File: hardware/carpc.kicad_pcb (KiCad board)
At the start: 2 copper layers, 47 parts, among them IC1 ATMEGA328-P, K3 CANBus, P1 PWR_IN, P2 MELBUS, P3 CONN_4, P4 RTI, P5 RELAY_OUT, Q1 BC547, Q2 RELAY, Q3 BC547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

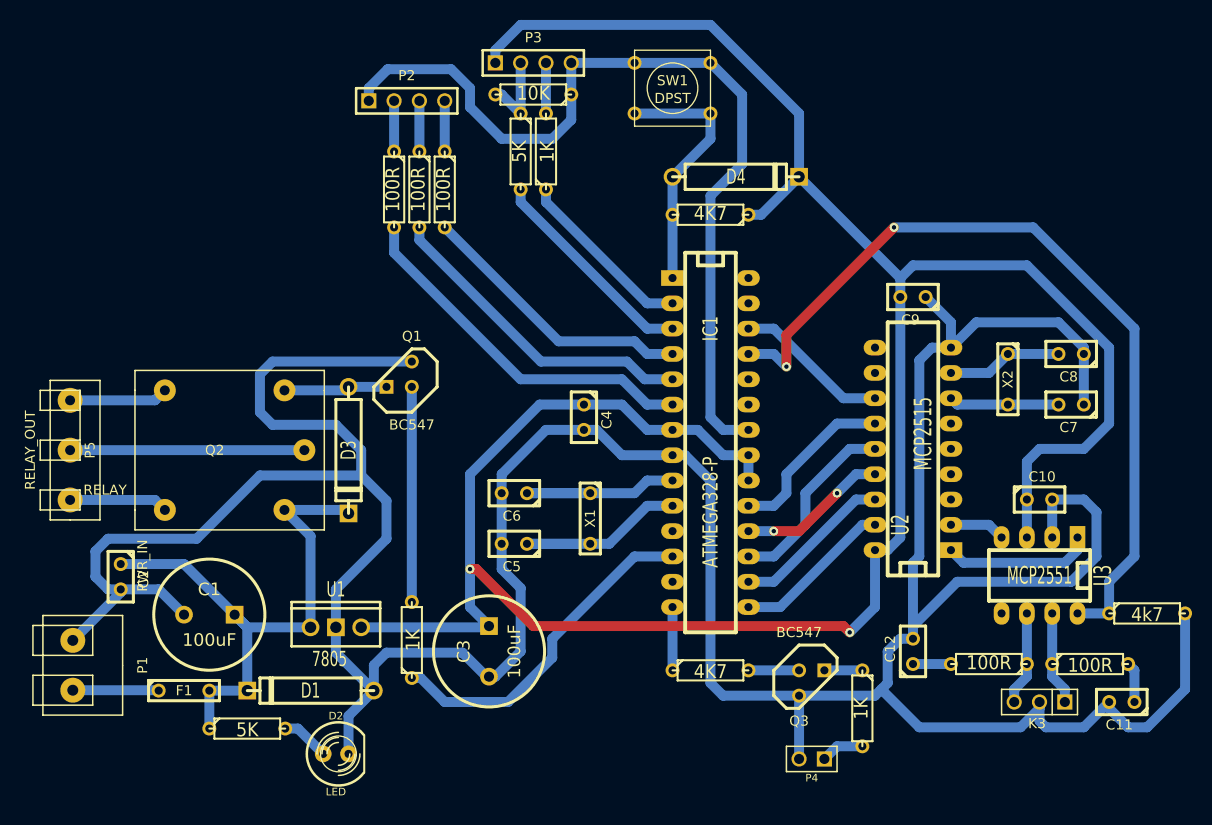
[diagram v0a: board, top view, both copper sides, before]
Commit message: Finished PCB layout
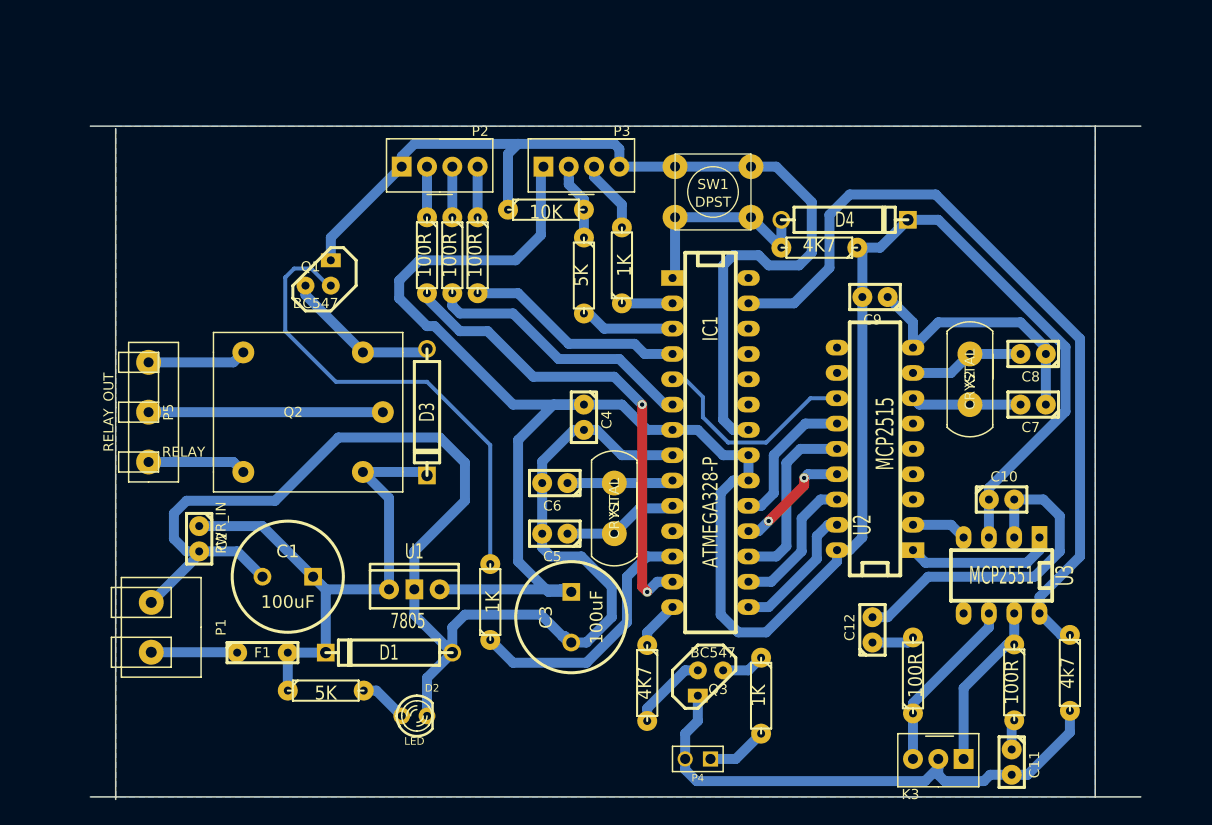
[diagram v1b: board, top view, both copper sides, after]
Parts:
- D2: footprint LED-5MM -> LED-3MM
- Q1, Q3: footprint TO92 -> TO92-CBE
- X1, X2: footprint C2 -> XTAL
- moved R9 14.0 mm to (109.2, 62.0)
- moved R13 13.7 mm to (113.0, 61.0)
- moved Q1 13.0 mm to (82.5, 61.7)
- moved C11 12.6 mm to (152.1, 110.8), turned to 270 degrees
- moved D4 11.7 mm to (135.4, 56.4)
- moved K3 11.7 mm to (144.8, 110.5)
- moved R10 11.6 mm to (105.4, 55.4), turned to 0 degrees
- moved P3 11.5 mm to (109.0, 51.1)
- moved P4 11.4 mm to (120.7, 110.5)
- moved R12 11.4 mm to (132.8, 59.2)
- moved SW1 11.2 mm to (122.2, 53.6)
- moved R14 10.2 mm to (127.0, 104.1)
- moved Q3 10.2 mm to (121.9, 102.9)
- moved R15 9.78 mm to (158.0, 101.9), turned to 270 degrees
- moved C3 8.94 mm to (108.0, 96.3)
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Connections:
- D3 pad 1: N-0000012 (its old number) -> N-000002
- IC1 pad 13: (no net) -> /MB_BUSY
- IC1 pad 25: CAN_STBY -> (no net)
- IC1 pad 26: CAN_WAKE -> (no net)
- IC1 pad 27: (no net) -> CAN_STBY
- IC1 pad 5: /MB_DATA -> CAN_WAKE
- IC1 pad 6: /MB_BUSY -> /MB_DATA
- Q2 pad 2: N-0000012 (its old number) -> N-000002
- R11 pad 2: N-0000036 -> N-0000037
- R14 pad 1: N-0000037 -> N-0000038
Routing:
- net GND: track 464.2 -> 356.5 mm
- net +5V: track 257.2 -> 223.8 mm, vias 2 -> 0
- net N-0000013: track 21.6 -> 48.3 mm
- net N-000002: track 0.00 -> 15.7 mm
- net /RXD: track 18.2 -> 5.08 mm
- net /TXD: track 21.8 -> 9.52 mm
- net /MB_BUSY: track 36.8 -> 48.5 mm, vias 0 -> 2
- net N-0000012 (its old number): track 10.4 -> 0.00 mm
- net N-0000040: track 21.3 -> 11.7 mm
- net N-0000039: track 20.2 -> 10.6 mm
- net N-0000057: track 9.42 -> 17.8 mm
- net /RELAY_OUT: track 34.3 -> 26.3 mm
- net N-0000056: track 9.42 -> 17.1 mm
- net CAN_WAKE: track 15.6 -> 22.2 mm
- net /MB_CLK: track 28.1 -> 22.1 mm
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- added copper zone on B.Cu, net GND
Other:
- board outline added: 105.4 x 67.6 mm
- net class Default: trace_width 0.254 -> 0.4
